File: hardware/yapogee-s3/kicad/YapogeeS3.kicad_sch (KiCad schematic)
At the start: 0 parts

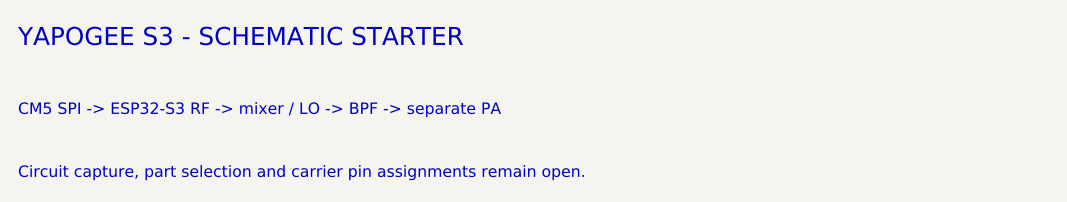
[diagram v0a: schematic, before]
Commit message: pick bare s3 parts
Add the daughterboard BOM and checked local symbols and footprints for the bare ESP32-S3R8, high-side RFFC5072A converter, driver and power interfaces. Keep sourcing and review notes private; circuit capture and RF qualification remain.
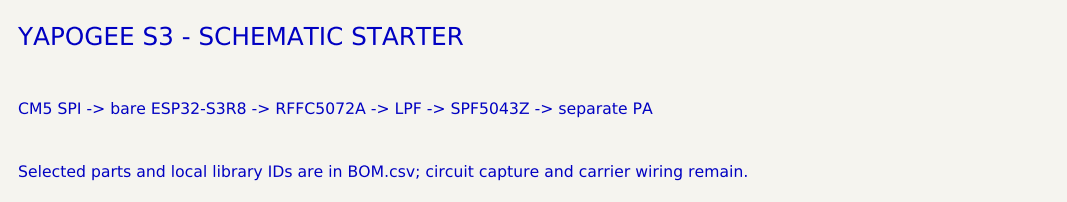
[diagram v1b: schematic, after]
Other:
- note added: "CM5 SPI -> bare ESP32-S3R8 -> RFFC5072A -> LPF -> SPF5043Z -> separate PA"
- note added: "Selected parts and local library IDs are in BOM.csv; circuit capture and carrier wiring remain."
- note removed: "CM5 SPI -> ESP32-S3 RF -> mixer / LO -> BPF -> separate PA"
- note removed: "Circuit capture, part selection and carrier pin assignments remain open."
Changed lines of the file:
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@@
   (title_block
     (title "Yapogee S3")
-    (date "2026-10-27")
+    (date "2026-10-28")
     (rev "Draft")
     (comment 1 "ESP32-S3 DVB-S2 frequency converter - nominal 5 V input")
@@
     (effects (font (size 2 2)) (justify left))
   )
-  (text "CM5 SPI -> ESP32-S3 RF -> mixer / LO -> BPF -> separate PA" (at 35 43 0)
+  (text "CM5 SPI -> bare ESP32-S3R8 -> RFFC5072A -> LPF -> SPF5043Z -> separate PA" (at 35 43 0)
     (effects (font (size 1.27 1.27)) (justify left))
   )
-  (text "Circuit capture, part selection and carrier pin assignments remain open." (at 35 50 0)
+  (text "Selected parts and local library IDs are in BOM.csv; circuit capture and carrier wiring remain." (at 35 50 0)
     (effects (font (size 1.27 1.27)) (justify left))
   )

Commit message: adopt WROOM RF module and quiet 3V supply
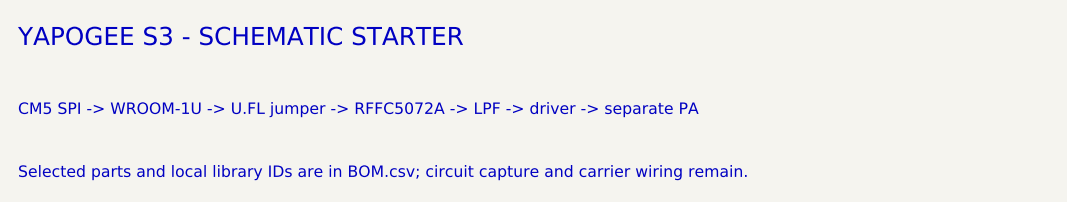
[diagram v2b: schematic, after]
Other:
- note added: "CM5 SPI -> WROOM-1U -> U.FL jumper -> RFFC5072A -> LPF -> driver -> separate PA"
- note removed: "CM5 SPI -> bare ESP32-S3R8 -> RFFC5072A -> LPF -> SPF5043Z -> separate PA"
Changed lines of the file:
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@@
     (effects (font (size 2 2)) (justify left))
   )
-  (text "CM5 SPI -> bare ESP32-S3R8 -> RFFC5072A -> LPF -> SPF5043Z -> separate PA" (at 35 43 0)
+  (text "CM5 SPI -> WROOM-1U -> U.FL jumper -> RFFC5072A -> LPF -> driver -> separate PA" (at 35 43 0)
     (effects (font (size 1.27 1.27)) (justify left))
   )
